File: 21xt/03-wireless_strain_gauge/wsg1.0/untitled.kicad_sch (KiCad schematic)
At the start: 3 parts

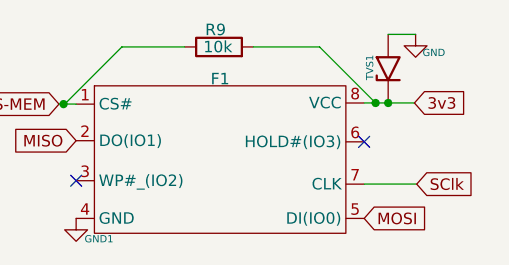
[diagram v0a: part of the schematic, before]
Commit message: Full v2 schematic and layout of WSG
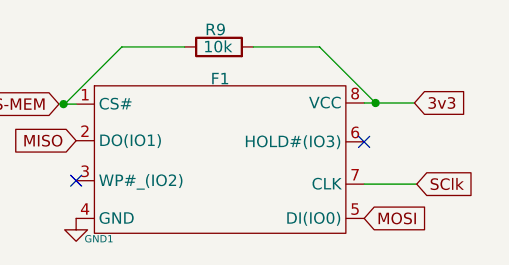
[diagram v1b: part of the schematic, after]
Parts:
- removed TVS1: 1.5KExxA, Diode_SMD:D_0603_1608Metric, symbol Diode:1.5KExxA
- R9: footprint Resistor_SMD:R_0603_1608Metric -> Resistor_SMD:R_0402_1005Metric
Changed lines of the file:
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@@
   (junction (at 87.63 61.087) (diameter 0) (color 0 0 0 0)
-  )
-  (junction (at 123.698 60.96) (diameter 0) (color 0 0 0 0)
   )
   (no_connect (at 121.031 65.278))
@@
     (stroke (width 0) (type default))
   )
-  (wire (pts (xy 123.698 60.96) (xy 122.301 60.96))
+  (wire (pts (xy 122.301 60.96) (xy 126.619 60.96))
     (stroke (width 0) (type default))
   )
   (wire (pts (xy 101.092 54.737) (xy 94.107 54.737))
-    (stroke (width 0) (type default))
-  )
-  (wire (pts (xy 126.619 60.96) (xy 123.698 60.96))
-    (stroke (width 0) (type default))
-  )
-  (wire (pts (xy 123.698 53.34) (xy 126.746 53.34))
     (stroke (width 0) (type default))
   )
@@
     )
   )
-  (symbol (lib_id "power:GND") (at 126.746 53.34 0) (unit 1)
-    (in_bom yes) (on_board yes) (dnp no)
-    (property "Reference" "#PWR023" (at 126.746 59.69 0)
-      (effects (font (size 1.27 1.27)) hide)
-    )
-    (property "Value" "GND" (at 128.778 55.372 0)
-      (effects (font (size 0.8 0.8)))
-    )
-    (property "Footprint" "" (at 126.746 53.34 0)
-      (effects (font (size 1.27 1.27)) hide)
-    )
-    (property "Datasheet" "" (at 126.746 53.34 0)
-      (effects (font (size 1.27 1.27)) hide)
-    )
-    (pin "1")
-    (instances
-      (project "wsg1.0"
-        (path "/03d0b5d1-0ab9-423a-b590-16c43c121de7"
-          (reference "#PWR023") (unit 1)
-        )
-        (path "/03d0b5d1-0ab9-423a-b590-16c43c121de7/d4cc5d07-d36d-400e-a1e4-f16f9f77e7c2"
-          (reference "#PWR030") (unit 1)
-        )
-      )
-    )
-  )
   (symbol (lib_id "Device:R") (at 104.902 54.737 90) (unit 1)
     (in_bom yes) (on_board yes) (dnp no)
@@
       (effects (font (size 1.27 1.27)))
     )
-    (property "Footprint" "Resistor_SMD:R_0603_1608Metric" (at 104.902 56.515 90)
+    (property "Footprint" "Resistor_SMD:R_0402_1005Metric" (at 104.902 56.515 90)
       (effects (font (size 1.27 1.27)) hide)
     )
@@
         )
       )
-    )
-  )
-  (symbol (lib_id "Diode:1.5KExxA") (at 123.698 57.15 90) (unit 1)
-    (in_bom yes) (on_board yes) (dnp no)
-    (property "Reference" "TVS1" (at 121.666 58.42 0)
-      (effects (font (size 0.8 0.8)) (justify left))
-    )
-    (property "Value" "1.5KExxA" (at 120.904 55.88 90)
-      (effects (font (size 1.27 1.27)) (justify left) hide)
-    )
-    (property "Footprint" "Diode_SMD:D_0603_1608Metric" (at 128.778 57.15 0)
-      (effects (font (size 1.27 1.27)) hide)
-    )
-    (property "Datasheet" "https://www.vishay.com/docs/88301/15ke.pdf" (at 123.698 58.42 0)
-      (effects (font (size 1.27 1.27)) hide)
-    )
-    (pin "1")
-    (pin "2")
-    (instances
-      (project "wsg1.0"
-        (path "/03d0b5d1-0ab9-423a-b590-16c43c121de7"
-          (reference "TVS1") (unit 1)
-        )
-        (path "/03d0b5d1-0ab9-423a-b590-16c43c121de7/d4cc5d07-d36d-400e-a1e4-f16f9f77e7c2"
-          (reference "TVS2") (unit 1)
-        )
-      )

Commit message: light comments
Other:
- note added: "expose these pads as something we can jump to if needed, or better yet figure out with travis if these need to be pulled up or down. im pretty sure the write protection needs to be held so that we can actually save to this, and the hold probably needs some sort of access. these do not need to be high frequency as they are just on off also the chip select probably does not need to be high speed ei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"
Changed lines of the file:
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@@
     (stroke (width 0) (type default))
+  )
+  (arc (start 63.5 -10.16) (mid 87.1194 21.7176) (end 81.28 60.96)
+    (stroke (width 0) (type default))
+    (fill (type none))
+  )
+  (text "expose these pads as something we can jump to if needed,\n or better yet figure out with travis if these need to\n be pulled up or down.\n\nim pretty sure the write protection needs to be held\nso that we can actually save to this, and the hold \nprobably needs some sort of access.\nthese do not need to be high frequency as they are just\non off\n\nalso the chip select probably does not need to be high\nspeed either"
+    (at 67.31 -7.62 0)
+    (effects (font (size 1.27 1.27)) (justify left bottom))
   )
   (global_label "SClk" (shape input) (at 126.873 69.977 0) (fields_autoplaced)
@@
   (symbol (lib_id "power:GND1") (at 89.027 73.787 0) (unit 1)
     (in_bom yes) (on_board yes) (dnp no)
-    (property "Reference" "#PWR029" (at 89.027 80.137 0)
+    (property "Reference" "#PWR031" (at 89.027 80.137 0)
       (effects (font (size 1.27 1.27)) hide)
     )
@@
     (instances
       (project "wsg1.0"
-        (path "/03d0b5d1-0ab9-423a-b590-16c43c121de7"
-          (reference "#PWR029") (unit 1)
-        )
         (path "/03d0b5d1-0ab9-423a-b590-16c43c121de7/d4cc5d07-d36d-400e-a1e4-f16f9f77e7c2"
           (reference "#PWR031") (unit 1)

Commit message: wsg redu
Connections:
- net SClk renamed SCLk
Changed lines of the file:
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@@
     (effects (font (size 1.27 1.27)) (justify left bottom))
   )
-  (global_label "SClk" (shape input) (at 126.873 69.977 0) (fields_autoplaced)
+  (global_label "SCLk" (shape input) (at 126.873 69.977 0) (fields_autoplaced)
     (effects (font (size 1.27 1.27)) (justify left))
-    (property "Intersheetrefs" "${INTERSHEET_REFS}" (at 134.031 69.977 0)
+    (property "Intersheetrefs" "${INTERSHEET_REFS}" (at 134.3939 69.977 0)
       (effects (font (size 1.27 1.27)) (justify left) hide)
     )
@@
     )
   )
-  (global_label "MISO" (shape input) (at 89.027 65.151 180) (fields_autoplaced)
+  (global_label "MISO" (shape output) (at 89.027 65.151 180) (fields_autoplaced)
     (effects (font (size 1.27 1.27)) (justify right))
     (property "Intersheetrefs" "${INTERSHEET_REFS}" (at 81.4456 65.151 0)
